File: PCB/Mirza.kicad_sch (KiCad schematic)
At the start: 95 parts, among them J1 In, J2 Out, J3 Power, Q1 BCM857DS, Q13 2SC3324, Q14 2SA1312, Q15 2SA1312, Q16 2SA1312, Q17 2SC3324, Q18 2SC3324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

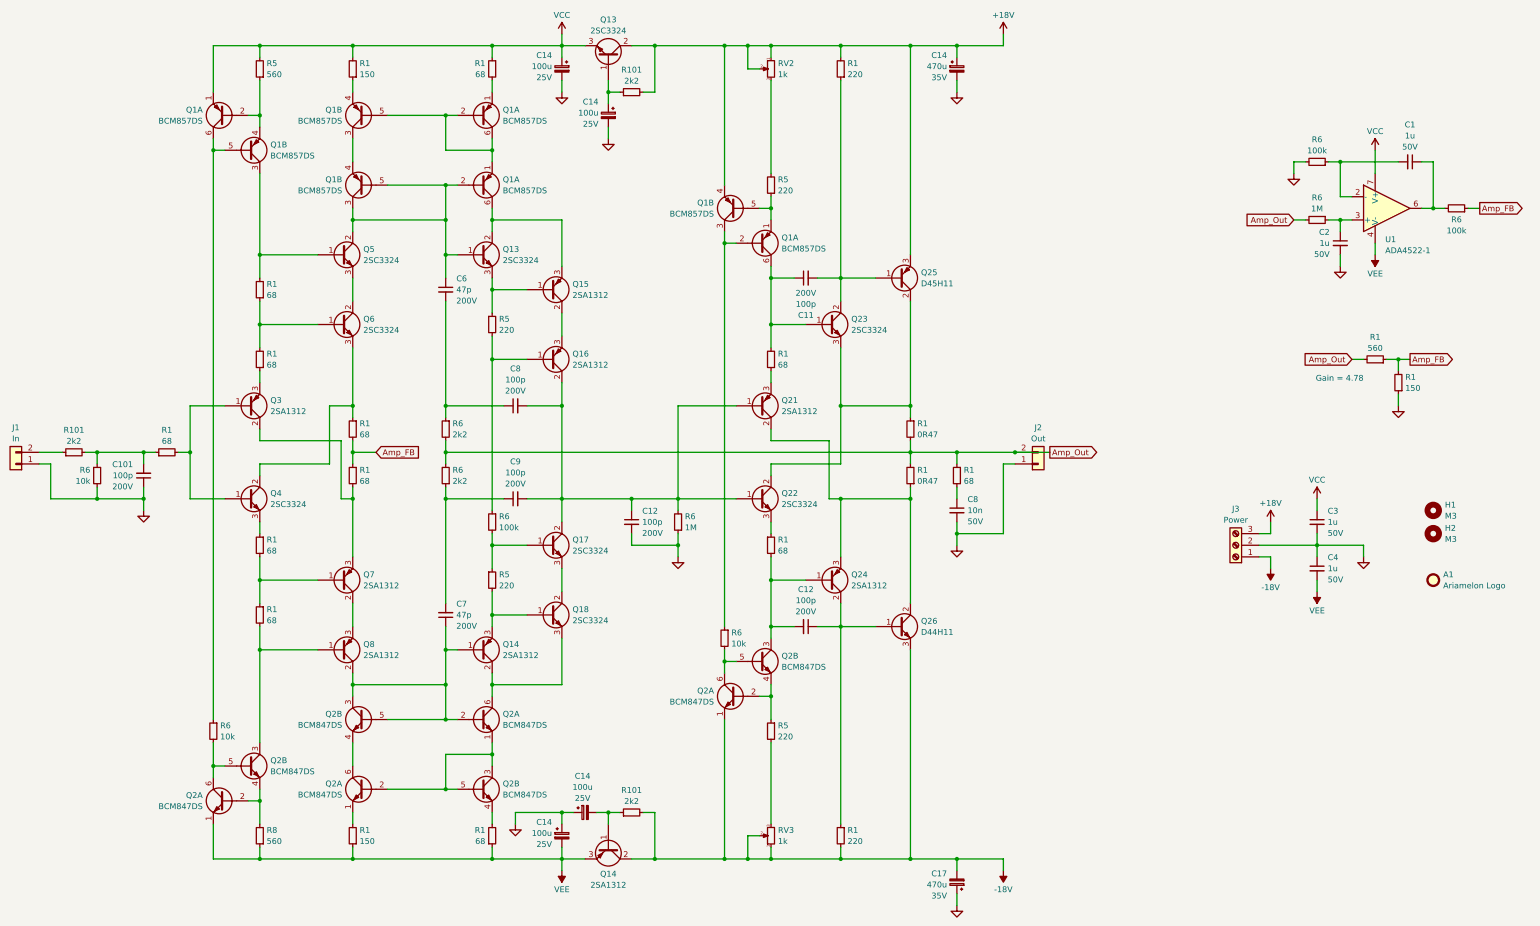
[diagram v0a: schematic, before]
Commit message: 05/10/2023 update
Changed input voltage to 15V.
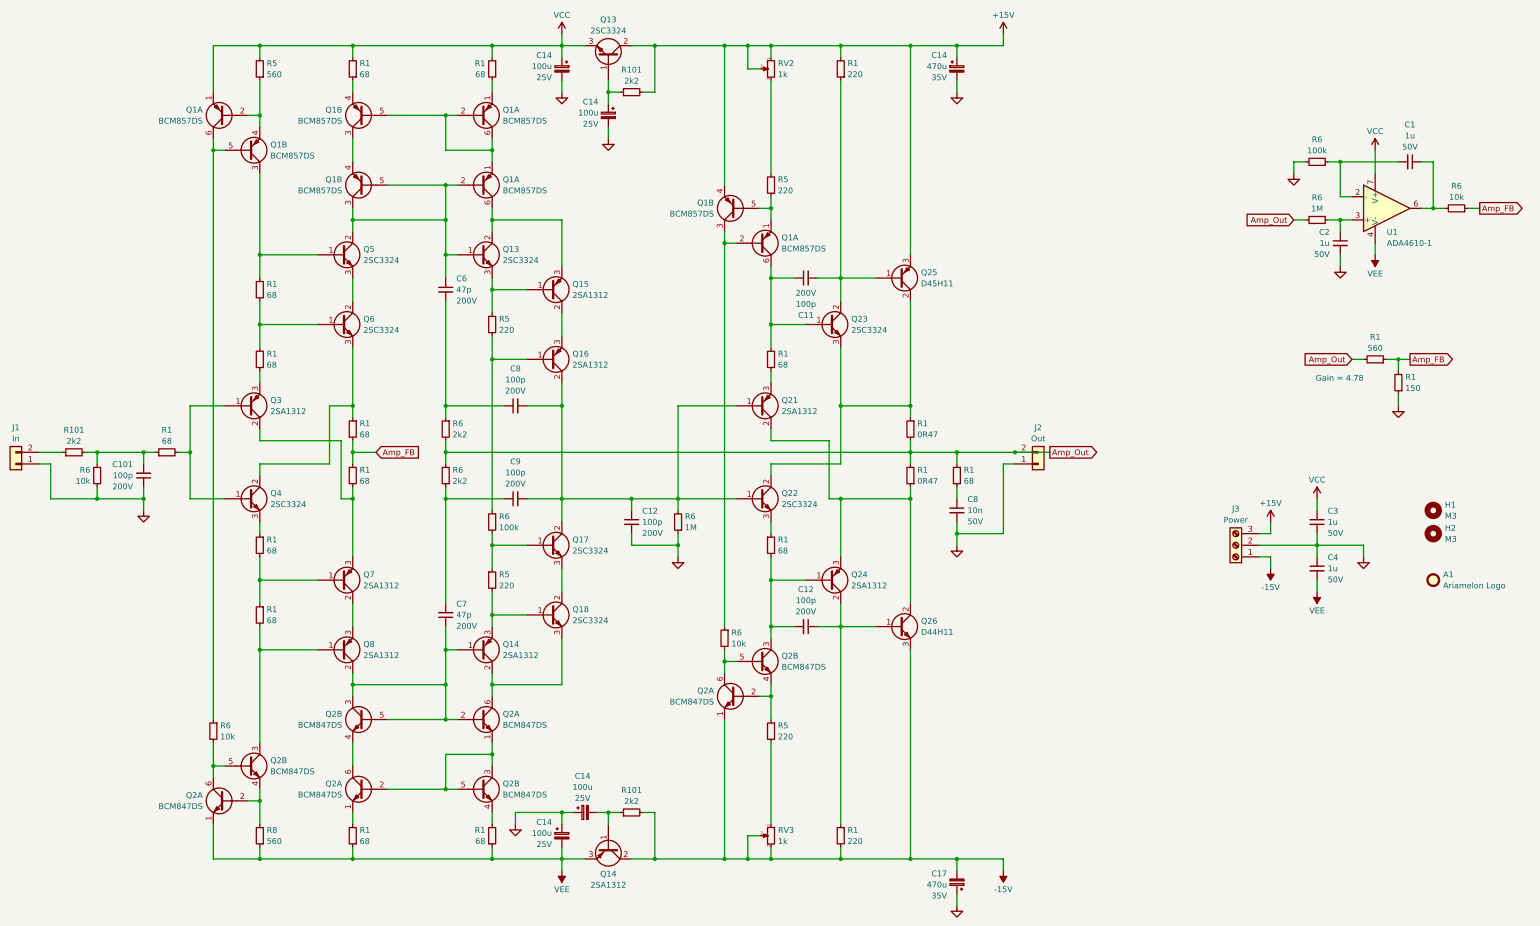
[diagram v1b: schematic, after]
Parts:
- removed R1 (x2): 150, Resistor_SMD:R_MiniMELF_MMA-0204, symbol Device:R_Small
- added R1 (x2): 68, Resistor_SMD:R_MiniMELF_MMA-0204, symbol Device:R_Small
- R6: value 100k -> 10k; LCSC C2836210 -> C2084764; Manufacturer No. MMA02040C1003FB300 -> MMA02040C1002FB300
- U1: value ADA4522-1 -> ADA4610-1; LCSC C160794 -> (none); Manufacturer No. ADA4522-1ARZ-R7 -> ADA4610-1ARZ-R7
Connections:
- net VCC: now also R1.2
- net VEE: now also R1.1
- net at Q1.4 (E2): now also R1.1
- net at Q2.1 (E1): now also R1.2
- net +18V renamed +15V
- net -18V renamed -15V
